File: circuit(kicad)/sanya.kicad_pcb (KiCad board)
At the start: 2 copper layers, 34.4 x 27.8 mm, 10 parts, among them J1 Oled, J2 Micro_SD_Card, SW1 Up, SW2 Down, SW3 Set, SW4 SW_DPDT_x2, U1 ATmega328P-A

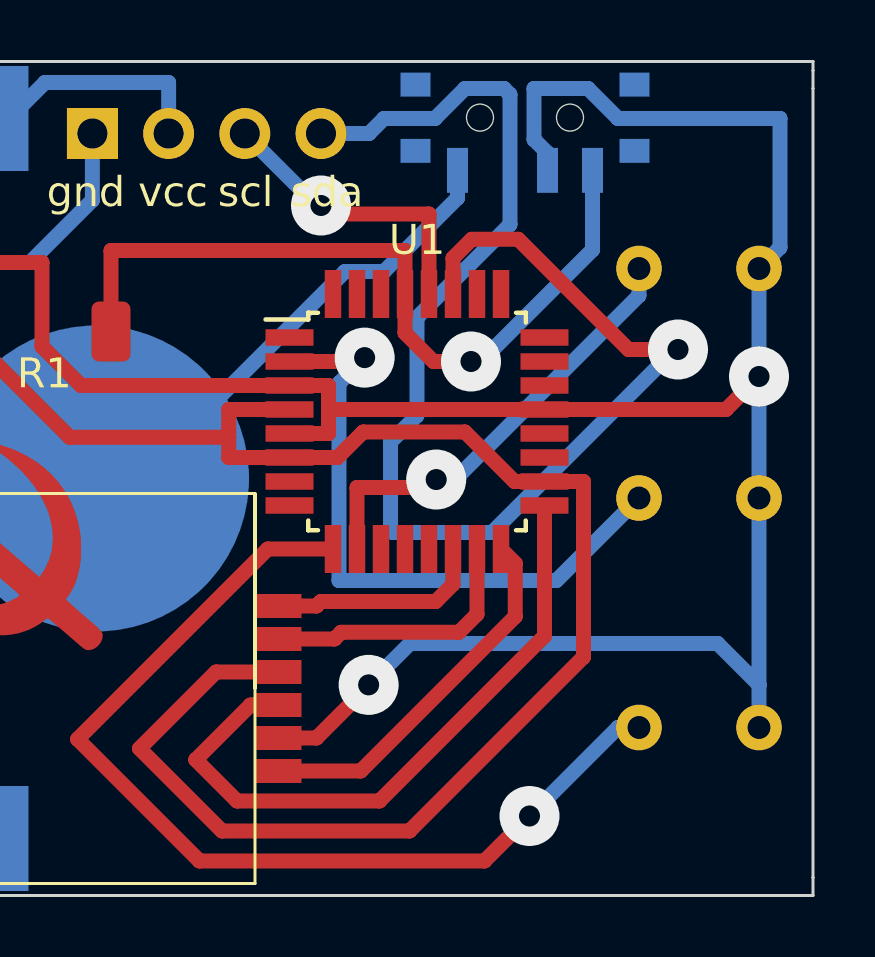
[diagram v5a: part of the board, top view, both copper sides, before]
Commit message: изменил посадочное под выключатель
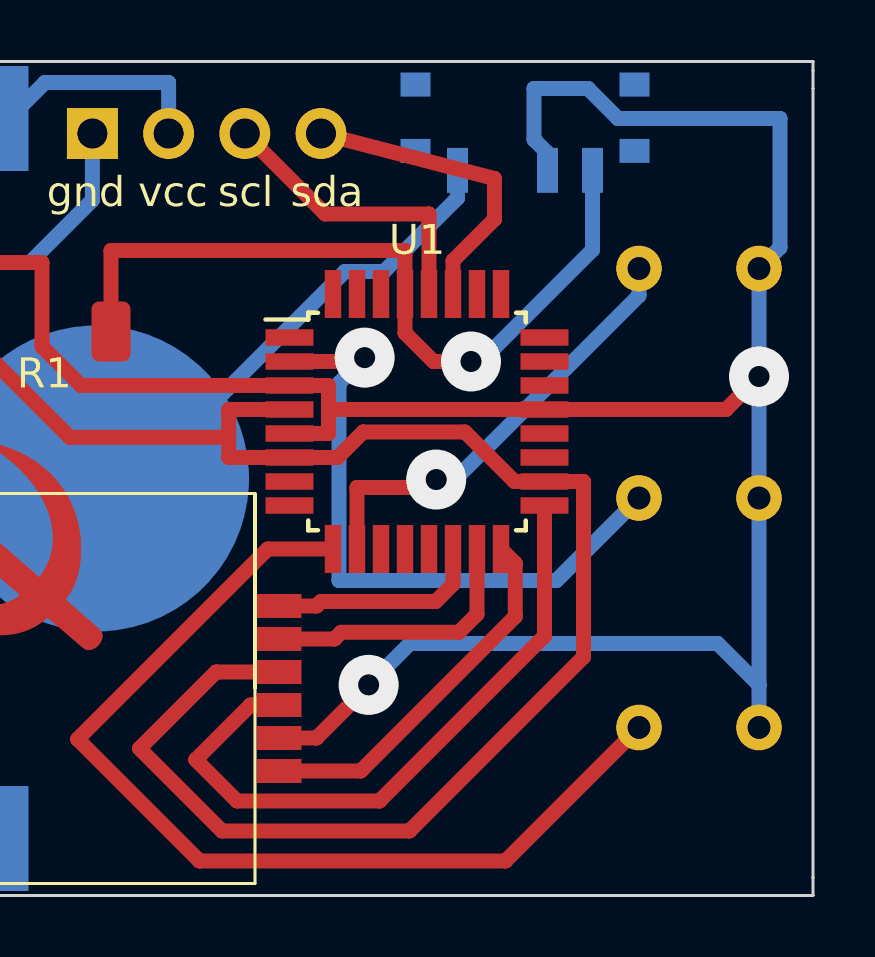
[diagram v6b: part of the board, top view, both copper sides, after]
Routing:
- net /SDA: track 45.8 -> 10.4 mm, vias 1 -> 0
- net /SCL: vias 1 -> 0
- net /PD5: vias 1 -> 0
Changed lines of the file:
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@@
     (property "ki_keywords" "switch dual-pole double-throw DPDT spdt ON-ON")
     (attr smd)
-    (fp_text reference "SW4" (at 0 3.2) (layer "B.SilkS")
-        (effects (font (size 1 1) (thickness 0.15)) (justify mirror))
-    )
-    (fp_text value "SW_DPDT_x2" (at 0 -4.25) (layer "B.Fab")
-        (effects (font (size 1 1) (thickness 0.15)) (justify mirror))
-    )
-    (fp_text user "${REFERENCE}" (at 0 3.2) (layer "B.Fab")
+    (fp_text reference "SW4" (at 0 3.2 180) (layer "B.SilkS")
+        (effects (font (size 1 1) (thickness 0.15)) (justify mirror))
+    )
+    (fp_text value "SW_DPDT_x2" (at 0 -4.25 180) (layer "B.Fab")
+        (effects (font (size 1 1) (thickness 0.15)) (justify mirror))
+    )
+    (fp_text user "${REFERENCE}" (at 0 3.2 180) (layer "B.Fab")
         (effects (font (size 1 1) (thickness 0.15)) (justify mirror))
     )
@@
     (pad "" smd rect (at -3.65 -1.43) (size 1 0.8) (layers "B.Cu" "B.Paste" "B.Mask"))
     (pad "" smd rect (at -3.65 0.78) (size 1 0.8) (layers "B.Cu" "B.Paste" "B.Mask"))
-    (pad "" np_thru_hole circle (at -1.5 -0.33) (size 0.9 0.9) (drill 0.9) (layers "*.Cu" "*.Mask"))
-    (pad "" np_thru_hole circle (at 1.5 -0.33) (size 0.9 0.9) (drill 0.9) (layers "*.Cu" "*.Mask"))
     (pad "" smd rect (at 3.65 -1.43) (size 1 0.8) (layers "B.Cu" "B.Paste" "B.Mask"))
     (pad "" smd rect (at 3.65 0.78) (size 1 0.8) (layers "B.Cu" "B.Paste" "B.Mask"))
@@
   (segment (start 154.18 59.22) (end 154.18 57) (width 0.5) (layer "B.Cu") (net 1))
   (segment (start 176.4 61.5) (end 176.4 65.1) (width 0.5) (layer "B.Cu") (net 1))
-  (segment (start 173.7 64.2) (end 172.05 64.2) (width 0.5) (layer "F.Cu") (net 2))
-  (segment (start 166.825 60.525) (end 166.2 61.15) (width 0.5) (layer "F.Cu") (net 2))
-  (segment (start 172.05 64.2) (end 168.375 60.525) (width 0.5) (layer "F.Cu") (net 2))
-  (segment (start 166.2 61.15) (end 166.2 62.35) (width 0.5) (layer "F.Cu") (net 2))
-  (segment (start 168.375 60.525) (end 166.825 60.525) (width 0.5) (layer "F.Cu") (net 2))
-  (via (at 173.7 64.2) (size 2) (drill 0.7) (layers "F.Cu" "B.Cu") (net 2))
-  (segment (start 161.8 57) (end 163.4 57) (width 0.5) (layer "B.Cu") (net 2))
-  (segment (start 165 66.4) (end 164.1178 67.2822) (width 0.5) (layer "B.Cu") (net 2))
-  (segment (start 165 63.1335) (end 165 66.4) (width 0.5) (layer "B.Cu") (net 2))
-  (segment (start 166.6 55.5) (end 167.9 55.5) (width 0.5) (layer "B.Cu") (net 2))
-  (segment (start 163.4 57) (end 163.9 56.5) (width 0.5) (layer "B.Cu") (net 2))
-  (segment (start 168.1 55.7) (end 168.1 60.0335) (width 0.5) (layer "B.Cu") (net 2))
-  (segment (start 165.6 56.5) (end 166.6 55.5) (width 0.5) (layer "B.Cu") (net 2))
-  (segment (start 164.1178 70.2178) (end 164.2 70.3) (width 0.5) (layer "B.Cu") (net 2))
-  (segment (start 163.9 56.5) (end 165.6 56.5) (width 0.5) (layer "B.Cu") (net 2))
-  (segment (start 173.6 64.2) (end 173.7 64.2) (width 0.5) (layer "B.Cu") (net 2))
-  (segment (start 167.5 70.3) (end 173.6 64.2) (width 0.5) (layer "B.Cu") (net 2))
-  (segment (start 164.2 70.3) (end 167.5 70.3) (width 0.5) (layer "B.Cu") (net 2))
-  (segment (start 168.1 60.0335) (end 165 63.1335) (width 0.5) (layer "B.Cu") (net 2))
-  (segment (start 164.1178 67.2822) (end 164.1178 70.2178) (width 0.5) (layer "B.Cu") (net 2))
-  (segment (start 167.9 55.5) (end 168.1 55.7) (width 0.5) (layer "B.Cu") (net 2))
-  (segment (start 162.083 59.683) (end 165.4 59.683) (width 0.5) (layer "F.Cu") (net 3))
-  (segment (start 161.8 59.4) (end 162.083 59.683) (width 0.5) (layer "F.Cu") (net 3))
+  (segment (start 161.8 57) (end 167.58 58.5) (width 0.5) (layer "F.Cu") (net 2))
+  (segment (start 166.2 61.24) (end 166.2 62.35) (width 0.5) (layer "F.Cu") (net 2))
+  (segment (start 167.58 58.5) (end 167.58 59.86) (width 0.5) (layer "F.Cu") (net 2))
+  (segment (start 167.58 59.86) (end 166.2 61.24) (width 0.5) (layer "F.Cu") (net 2))
+  (segment (start 161.943 59.683) (end 165.4 59.683) (width 0.5) (layer "F.Cu") (net 3))
+  (segment (start 159.26 57) (end 161.943 59.683) (width 0.5) (layer "F.Cu") (net 3))
   (segment (start 165.4 59.683) (end 165.4 62.35) (width 0.5) (layer "F.Cu") (net 3))
-  (via (at 161.8 59.4) (size 2) (drill 0.7) (layers "F.Cu" "B.Cu") (net 3))
-  (segment (start 161.66 59.4) (end 159.26 57) (width 0.5) (layer "B.Cu") (net 3))
-  (segment (start 161.8 59.4) (end 161.66 59.4) (width 0.5) (layer "B.Cu") (net 3))
   (segment (start 158.725 66.2) (end 158.725 67.125) (width 0.5) (layer "F.Cu") (net 4))
   (segment (start 153.425 67.125) (end 158.725 67.125) (width 0.5) (layer "F.Cu") (net 4))
@@
   (segment (start 165.6402 68.5347) (end 166.2653 68.5347) (width 0.5) (layer "B.Cu") (net 10))
   (segment (start 166.2653 68.5347) (end 172.4 62.4) (width 0.5) (layer "B.Cu") (net 10))
-  (segment (start 167.25 81.25) (end 157.75 81.25) (width 0.5) (layer "F.Cu") (net 11))
-  (segment (start 168.75 79.75) (end 167.25 81.25) (width 0.5) (layer "F.Cu") (net 11))
   (segment (start 160.025 70.85) (end 162.2 70.85) (width 0.5) (layer "F.Cu") (net 11))
+  (segment (start 167.95 81.25) (end 157.75 81.25) (width 0.5) (layer "F.Cu") (net 11))
+  (segment (start 157.75 81.25) (end 153.6875 77.1875) (width 0.5) (layer "F.Cu") (net 11))
+  (segment (start 172.4 76.8) (end 167.95 81.25) (width 0.5) (layer "F.Cu") (net 11))
   (segment (start 153.6875 77.1875) (end 160.025 70.85) (width 0.5) (layer "F.Cu") (net 11))
-  (segment (start 157.75 81.25) (end 153.6875 77.1875) (width 0.5) (layer "F.Cu") (net 11))
-  (via (at 168.75 79.75) (size 2) (drill 0.7) (layers "F.Cu" "B.Cu") (net 11))
-  (segment (start 168.75 79.75) (end 171.7 76.8) (width 0.5) (layer "B.Cu") (net 11))
-  (segment (start 171.7 76.8) (end 172.4 76.8) (width 0.5) (layer "B.Cu") (net 11))
   (segment (start 163.1249 64.6) (end 160.75 64.6) (width 0.5) (layer "F.Cu") (net 12))
   (segment (start 163.2544 64.4705) (end 163.1249 64.6) (width 0.5) (layer "F.Cu") (net 12))
@@
   (segment (start 166.35 58.23) (end 166.35 59.15) (width 0.5) (layer "B.Cu") (net 29))
   (segment (start 155.7 68.5) (end 154.3 68.5) (width 0.5) (layer "B.Cu") (net 29))
-  (zone (net 0) (net_name "") (layer "F.Cu") (hatch edge 0.5)
-    (connect_pads (clearance 0))
-    (min_thickness 0.25) (filled_areas_thickness no)
-    (keepout (tracks not_allowed) (vias not_allowed) (pads not_allowed) (copperpour allowed) (footprints allowed))
-    (fill (thermal_gap 0.5) (thermal_bridge_width 0.5))
-    (polygon
-      (pts
-        (xy 177.5 62.5)
-        (xy 177.5 60.5)
-        (xy 175.5 60.5)
-        (xy 175.5 62.5)
-      )
-    )
-  )
-  (zone (net 0) (net_name "") (layer "F.Cu") (hatch edge 0.5)
-    (connect_pads (clearance 0))
-    (min_thickness 0.25) (filled_areas_thickness no)
-    (keepout (tracks not_allowed) (vias not_allowed) (pads not_allowed) (copperpour allowed) (footprints allowed))
-    (fill (thermal_gap 0.5) (thermal_bridge_width 0.5))
-    (polygon
-      (pts
-        (xy 171.5 77.75)
-        (xy 171.5 75.75)
-        (xy 173.25 75.75)
-        (xy 173.25 77.75)
-      )
-    )
-  )
-  (zone (net 0) (net_name "") (layer "F.Cu") (hatch edge 0.5)
-    (connect_pads (clearance 0))
-    (min_thickness 0.25) (filled_areas_thickness no)
-    (keepout (tracks not_allowed) (vias not_allowed) (pads not_allowed) (copperpour allowed) (footprints allowed))
-    (fill (thermal_gap 0.5) (thermal_bridge_width 0.5))
-    (polygon
-      (pts
-        (xy 177.5 77.75)
-        (xy 177.5 75.75)
-        (xy 175.5 75.75)
-        (xy 175.5 77.75)
-      )
-    )
-  )
-  (zone (net 0) (net_name "") (layer "F.Cu") (hatch edge 0.5)
-    (connect_pads (clearance 0))
-    (min_thickness 0.25) (filled_areas_thickness no)
-    (keepout (tracks not_allowed) (vias not_allowed) (pads not_allowed) (copperpour allowed) (footprints allowed))
-    (fill (thermal_gap 0.5) (thermal_bridge_width 0.5))
-    (polygon
-      (pts
-        (xy 177.5 70)
-        (xy 177.5 68)
-        (xy 175.5 68)
-        (xy 175.5 70)
-      )
-    )
-  )
-  (zone (net 0) (net_name "") (layer "F.Cu") (hatch edge 0.5)
-    (connect_pads (clearance 0))
-    (min_thickness 0.25) (filled_areas_thickness no)
-    (keepout (tracks not_allowed) (vias allowed) (pads allowed) (copperpour allowed) (footprints allowed))
-    (fill (thermal_gap 0.5) (thermal_bridge_width 0.5))
-    (polygon
-      (pts
-        (xy 163.6 55.6)
-        (xy 152.4 55.6)
-        (xy 152.4 58.4)
-        (xy 163.6 58.4)
-      )
-    )
-  )
-  (zone (net 0) (net_name "") (layer "F.Cu") (hatch edge 0.5)
-    (connect_pads (clearance 0))
-    (min_thickness 0.25) (filled_areas_thickness no)
-    (keepout (tracks not_allowed) (vias not_allowed) (pads allowed) (copperpour allowed) (footprints allowed))
-    (fill (thermal_gap 0.5) (thermal_bridge_width 0.5))
-    (polygon
-      (pts
-        (xy 173.5 70.25)
-        (xy 173.5 68.25)
-        (xy 171.5 68.25)
-        (xy 171.5 70.25)
-      )
-    )
-  )
-  (zone (net 0) (net_name "") (layer "F.Cu") (hatch edge 0.5)
-    (connect_pads (clearance 0))
-    (min_thickness 0.25) (filled_areas_thickness no)
-    (keepout (tracks not_allowed) (vias not_allowed) (pads not_allowed) (copperpour allowed) (footprints allowed))
-    (fill (thermal_gap 0.5) (thermal_bridge_width 0.5))
-    (polygon
-      (pts
-        (xy 173.25 62.5)
-        (xy 173.25 60.5)
-        (xy 171.25 60.5)
-        (xy 171.25 62.5)
-      )
-    )
-  )
 )

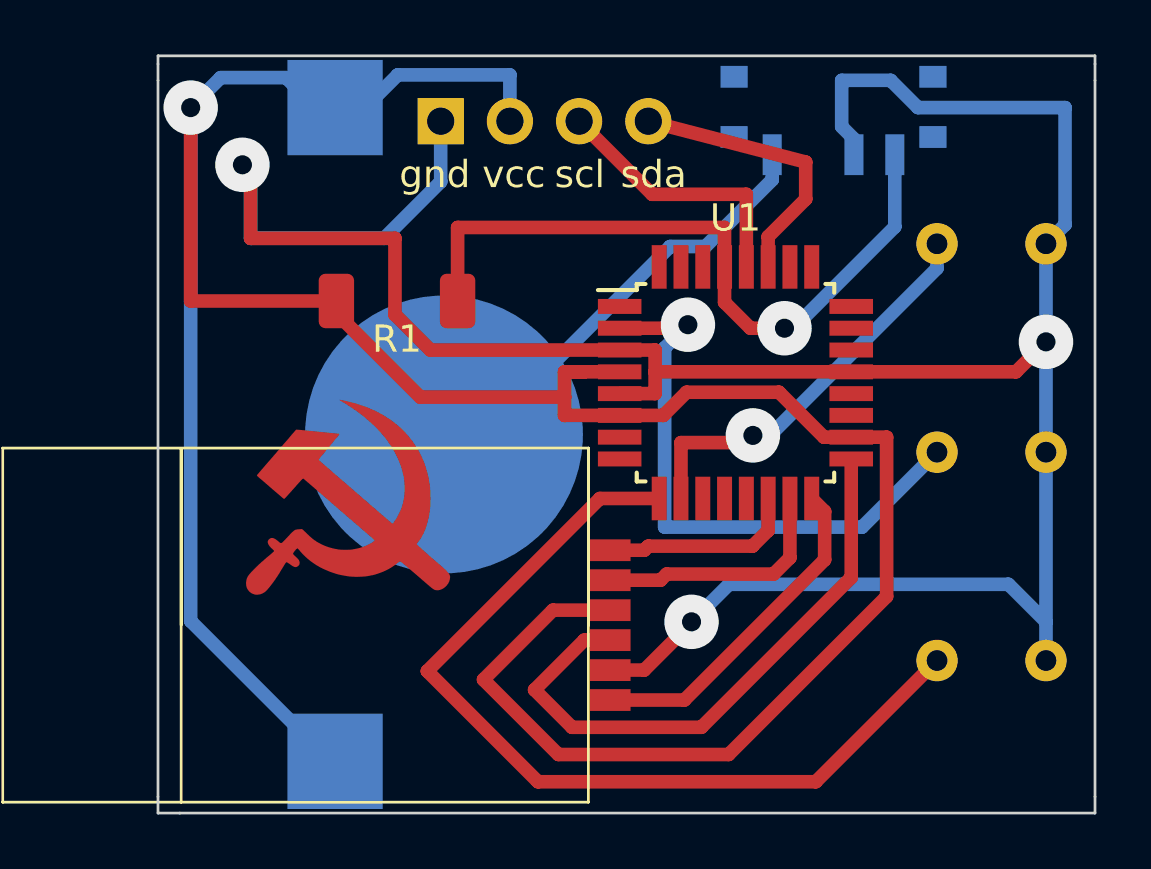
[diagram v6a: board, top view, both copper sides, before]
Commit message: Изменил посадочное место для батарейки; Заново протрассировал дорожки
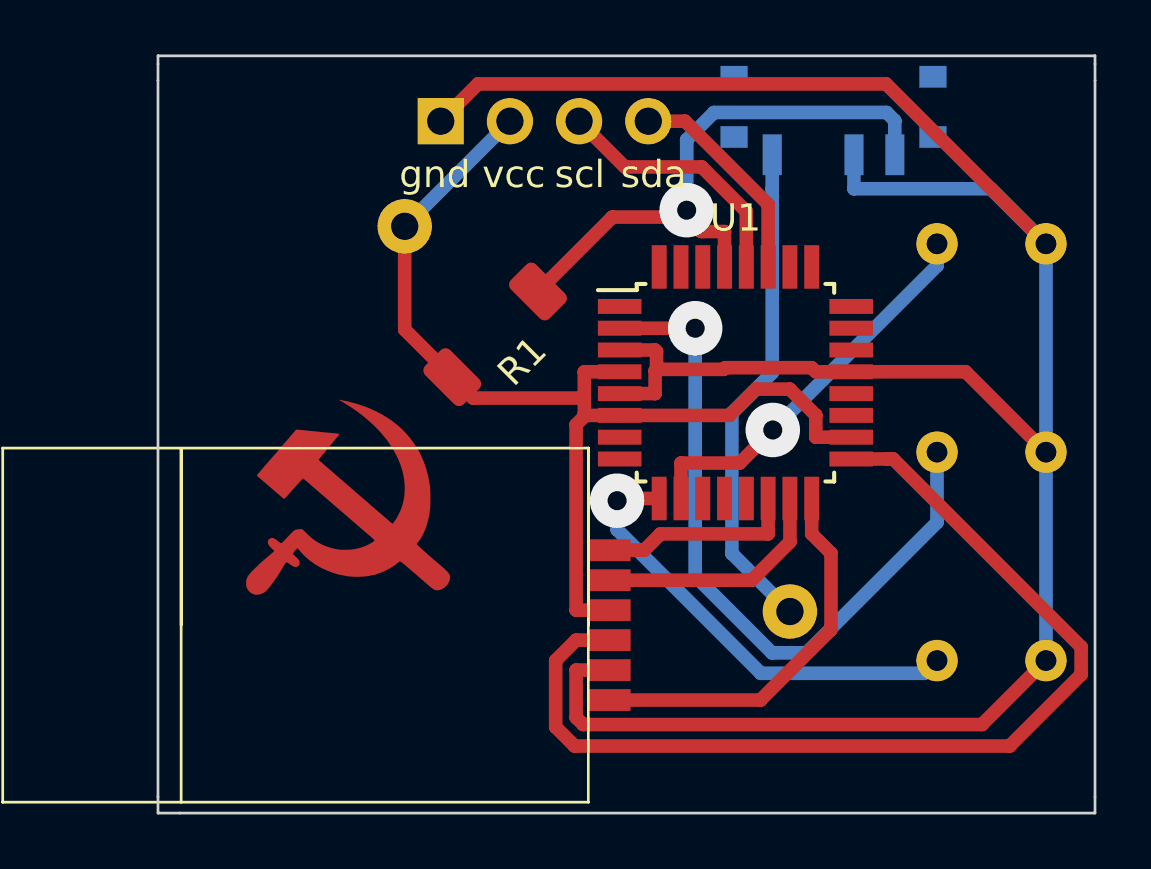
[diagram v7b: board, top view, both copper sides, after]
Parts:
- BT1: footprint Battery:BatteryHolder_Keystone_3000_1x12mm -> Library:CR2032_BatteryHolder
- moved BT1 5.01 mm to (155.7, 63.7), turned to 135 degrees
- moved R1 3.80 mm to (156.2, 64.8), turned to -135 degrees
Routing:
- net VCC: track 111.6 -> 39.7 mm, vias 1 -> 0
- net /PD5: track 33.4 -> 16.8 mm, vias 0 -> 1
- net /SCK: track 22.4 -> 37.7 mm
- net Earth: track 101.6 -> 90.8 mm, vias 3 -> 0
- net /PD4: track 21.5 -> 26.5 mm
- net /RST: track 26.1 -> 21.8 mm
- net /SDA: track 10.4 -> 7.96 mm
- net /MISO: track 12.5 -> 14.3 mm
- net Net-(BT1--): track 16.8 -> 18.3 mm

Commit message: подвигал дорожки, добавил лого :)
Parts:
- G***: moved to B.Cu
- moved G*** 15.5 mm to (141.2, 58.6), turned to 90 degrees
- moved J2 14.3 mm to (163.4, 61.8), turned to 0 degrees
- moved R1 10.2 mm to (147.8, 59.0)
- moved SW3 9.74 mm to (167.9, 61.9)
- moved J1 9.74 mm to (150.2, 49.8)
- moved SW1 9.74 mm to (167.9, 54.3)
- moved SW2 9.74 mm to (167.9, 69.6)
- moved U1 9.74 mm to (158.5, 59.4)
- moved BT1 9.62 mm to (148.9, 56.9)
- moved SW4 9.14 mm to (163.0, 49.5)
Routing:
- net /RST: track 21.8 -> 86.0 mm
- net VCC: track 39.7 -> 87.4 mm
- net /SCK: track 37.7 -> 66.4 mm
- net Earth: track 90.8 -> 115.2 mm
- net /PD5: track 16.8 -> 31.4 mm
- net /SCL: track 9.55 -> 0.00 mm
- net /SDA: track 7.96 -> 0.00 mm
- net /PD4: track 26.5 -> 33.2 mm
- net unconnected-(U1-XTAL2/PB7-Pad8): track 0.00 -> 3.89 mm
- net /MISO: track 14.3 -> 17.1 mm
- net Net-(BT1--): track 18.3 -> 19.4 mm
- net /MOSI: track 8.78 -> 9.72 mm
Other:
- board text added: "&"
- board text added: "I"
- board text added: "K"
- board text added: "O"
- board text added: "T"
